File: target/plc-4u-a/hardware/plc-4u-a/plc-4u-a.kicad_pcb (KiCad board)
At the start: 2 copper layers, 363.5 x 84 mm, 216 parts, among them J1 Screw_Terminal_01x02, J10 AUX_INS, J11 X Leds Btns, J12 S3 S5 LEDs, J13 Valve control in, J14 Leak sensors, J15 I2C, J16 I2C, J17 TA_C, J18 X leds btns, J19 Valve leds, J2 Screw_Terminal_01x02, J20 Valve leds, J21 Leak sensors, J22 Valve control in, J23 S3 S5 LEDs, J24 S4 S6 LEDs, J25 S3 S5 LEDs, J26 S4 S6 LEDs, J27 S3BTN, J28 S4BTN, J29 S5BTN, J3 Screw_Terminal_01x02, J30 S6BTN, J31 S3BTN, J32 S4BTN, J33 S5BTN, J34 S6BTN, J35 PWR_OUT, J36 Sensors AB, J37 Sensors CD, J38 PWR_OUT, J39 Leak sensors, J4 Screw_Terminal_01x02, J40 Leak sensors, J41 TA_C, J42 TB_C, J43 TC_C, J44 TD_C, J45 TB_C, J46 TC_C, J47 TD_C, J48 S3 S5 LEDs, J49 S1 S2 LEDs, J5 Screw_Terminal_01x02, J50 S1 S2 BTNS, J51 X0, J52 U8 IN, J53 X0, J54 X9 IN, J55 AVR-ISP-10, J56 U17 OUT, J57 U8 OUT, J58 U17 OUT, J59 U8 OUT, J6 V_ST_HWS, J60 GND, J61 GND, J62 VCC, J63 VCC, J64 SIM800, J65 RES_IN, J66 SELF_PWR_IN, J67 VDD VSS, J68 VDD VSS, J69 VDD, J7 V_ST_CWS, J70 VDD, J71 RESERVED_OUT, J72 VSS, J73 VSS, J74 VSS, J75 VSS, J76 VSS, J77 VDD, J78 VDD, J79 NC, J8 W_CT_HWS, J80 NC, J81 NC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

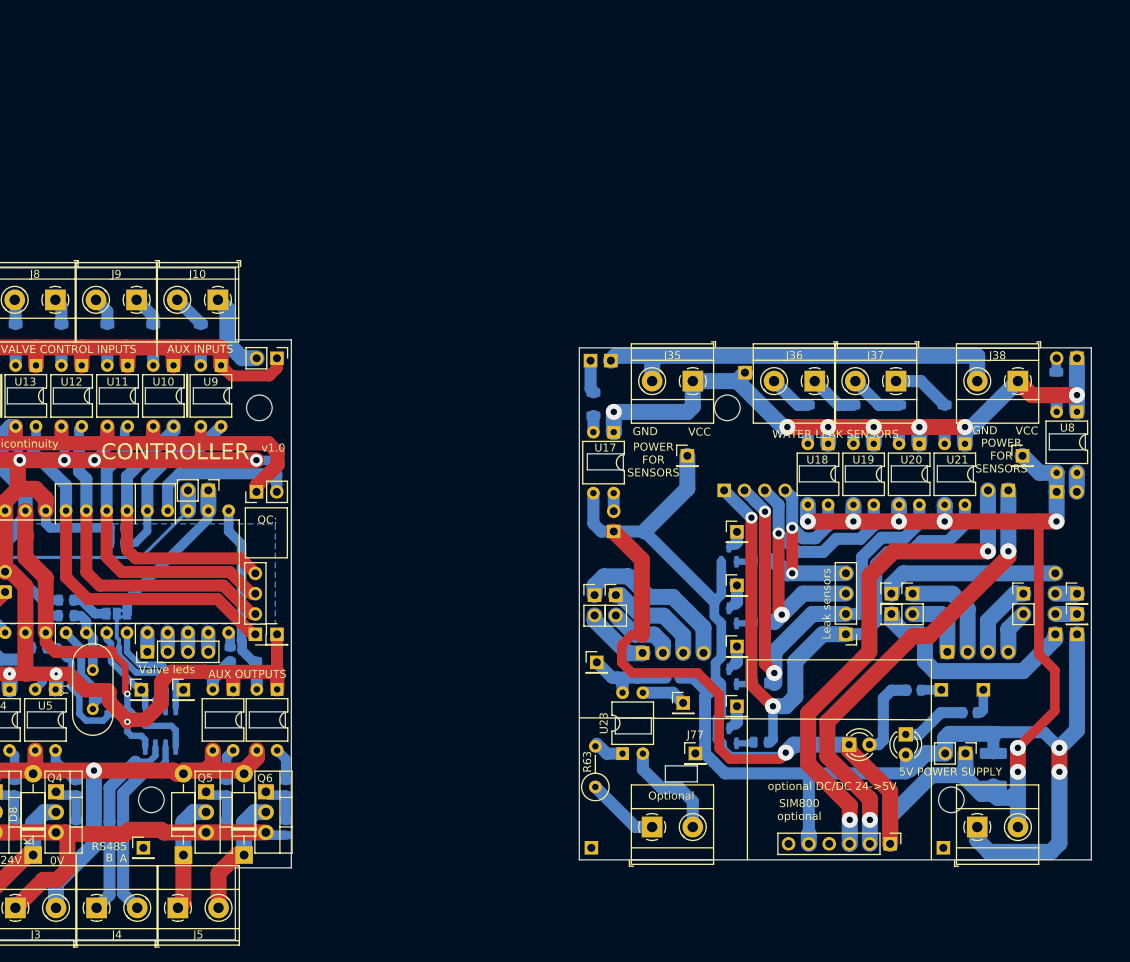
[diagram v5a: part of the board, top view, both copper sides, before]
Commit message: plc-4u-a board += RS485 protection
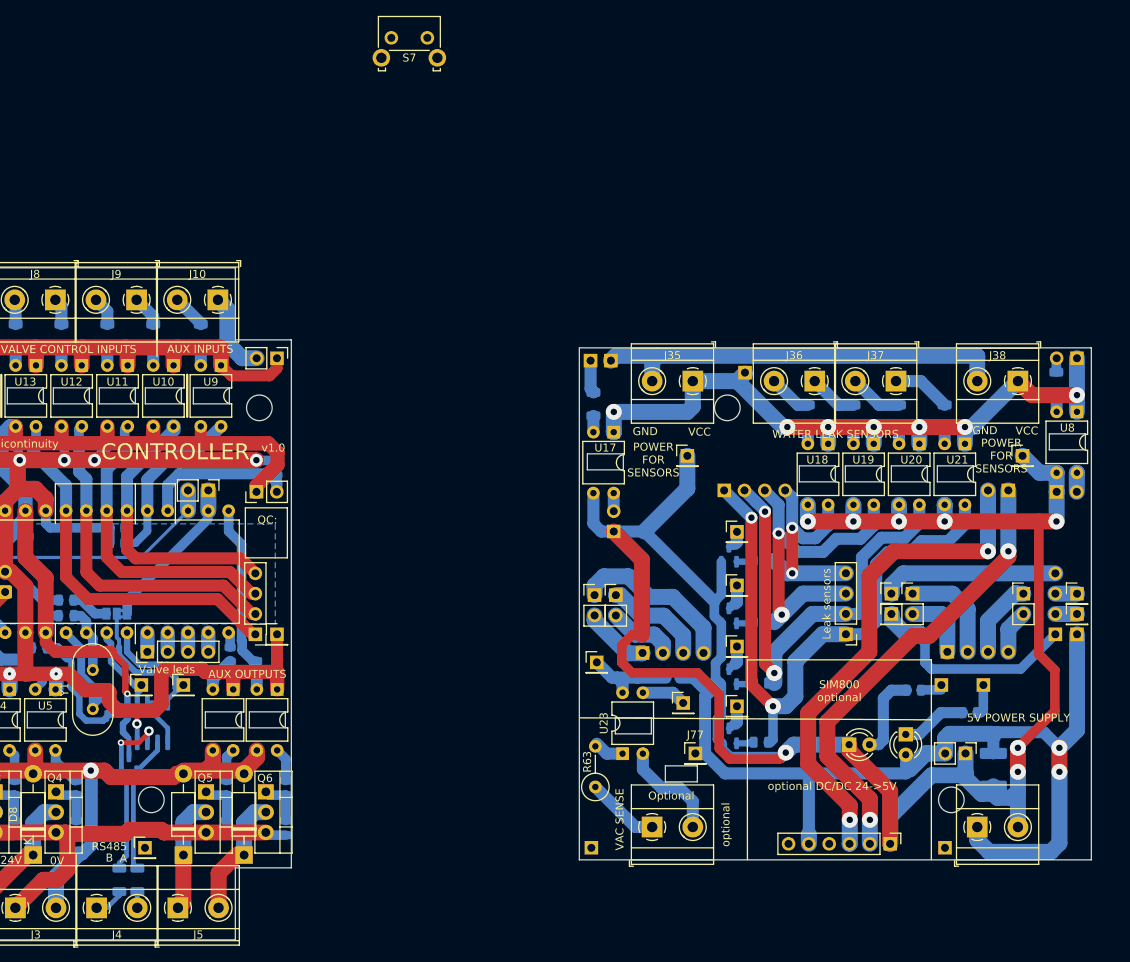
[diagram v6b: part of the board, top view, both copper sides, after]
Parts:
- added D13: PESD2CAN, Package_TO_SOT_SMD:SOT-23, B.Cu at (111.7, 120.0)
- added R66: 10, Resistor_SMD:R_1206_3216Metric, B.Cu at (112.8, 134.5)
- added R67: 10, Resistor_SMD:R_1206_3216Metric, B.Cu at (110.5, 134.5)
- added S7: MOMENTARY-SWITCH-SPST-PTH-6.0MM, Button_Switch_THT:SW_Tactile_SKHH_Angled, F.Cu at (144.5, 29.2)
- moved U22 1.17 mm to (114.6, 114.8)
- moved J83 0.60 mm to (113.2, 110.2)
- moved J84 0.60 mm to (213.2, 110.2)
- moved J85 0.60 mm to (118.5, 110.2)
- moved J86 0.60 mm to (218.5, 110.2)
- moved J81 0.20 mm to (113.7, 130.5)
- moved J82 0.20 mm to (213.7, 130.5)
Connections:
- U22 pad 6: /A -> /AA
- U22 pad 7: /B -> /BB
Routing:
- net /BB: track 0.00 -> 22.0 mm, vias 0 -> 2
- net /A: track 23.8 -> 2.04 mm
- net /B: track 24.2 -> 3.97 mm
- net /AA: track 0.00 -> 17.2 mm
- net /VSS: track 232.2 -> 239.8 mm
- net /VDD: track 206.4 -> 205.2 mm
- net Net-(JP1-Pad2): track 18.1 -> 17.1 mm
- net /TXD: track 13.8 -> 13.1 mm
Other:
- board text added: "VAC SENSE"
- board text added: "optional"

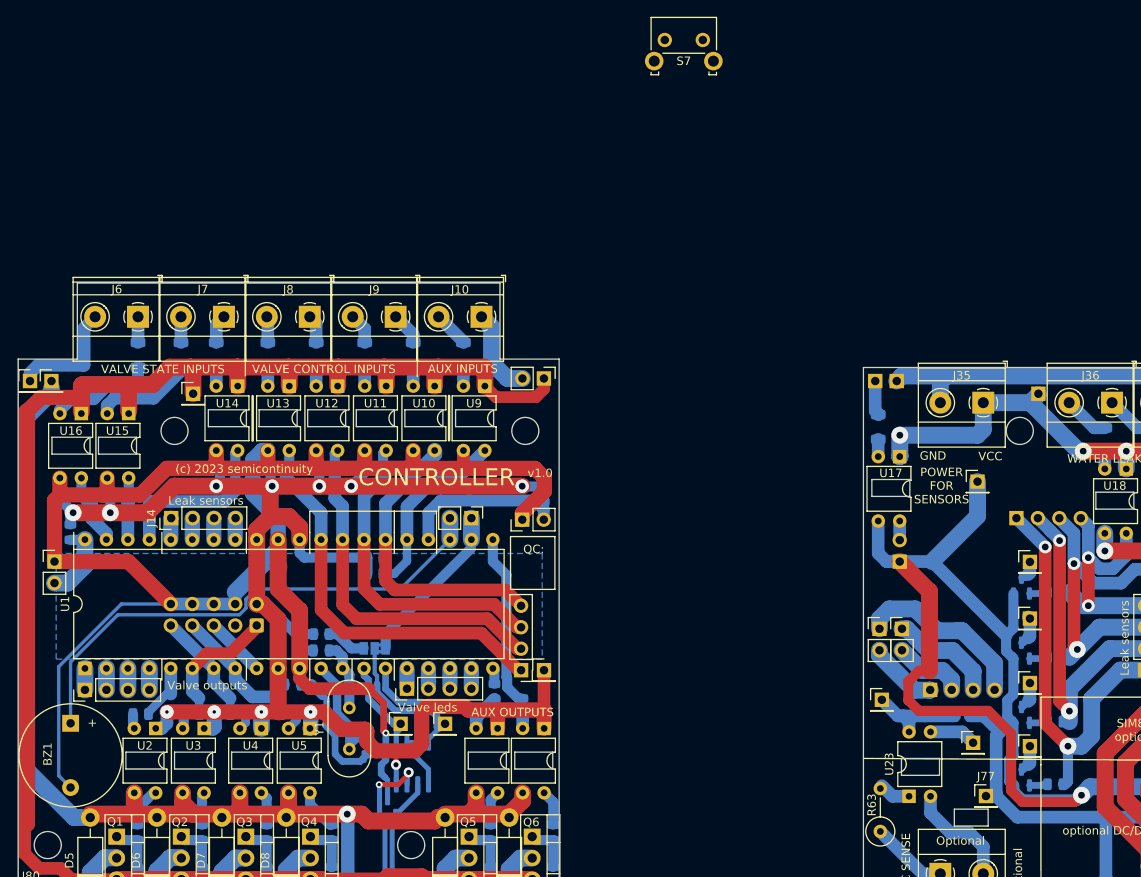
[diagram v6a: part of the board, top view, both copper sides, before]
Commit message: plc4u-a: main-retained-register (preparing for buzzer)
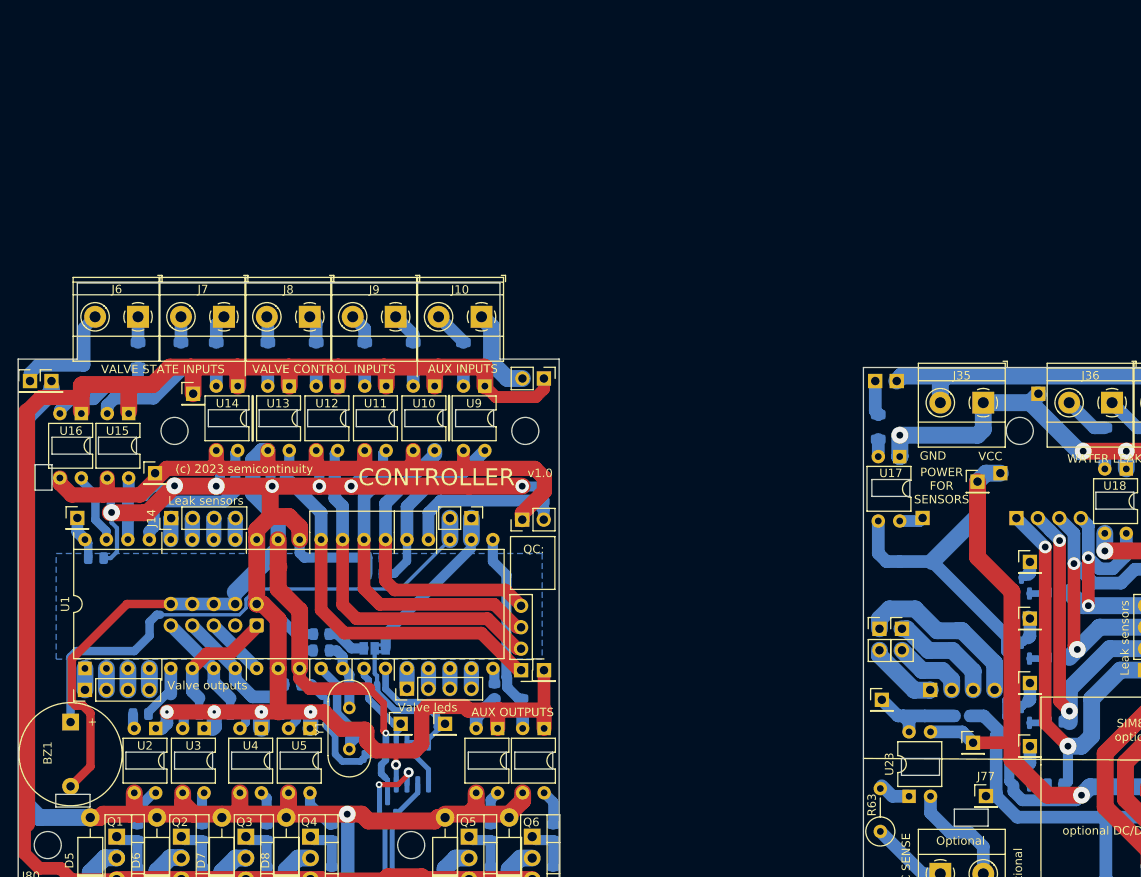
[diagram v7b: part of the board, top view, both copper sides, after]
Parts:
- removed S7: MOMENTARY-SWITCH-SPST-PTH-6.0MM, Button_Switch_THT:SW_Tactile_SKHH_Angled
- added J87: VSS, Connector_PinHeader_2.54mm:PinHeader_1x01_P2.54mm_Vertical, F.Cu at (84.2, 80.5)
- added J88: VSS, Connector_PinHeader_2.54mm:PinHeader_1x01_P2.54mm_Vertical, B.Cu at (184.2, 80.5)
- J56: value U17 OUT -> PA0; footprint Connector_PinHeader_2.54mm:PinHeader_1x02_P2.54mm_Vertical -> Connector_PinHeader_2.54mm:PinHeader_1x01_P2.54mm_Vertical
- J58: value U17 OUT -> NC; footprint Connector_PinHeader_2.54mm:PinHeader_1x02_P2.54mm_Vertical -> Connector_PinHeader_2.54mm:PinHeader_1x01_P2.54mm_Vertical
- J71: value RESERVED_OUT -> RESERVED_IN
- moved J56 5.83 mm to (175.0, 85.8), turned to 180 degrees
- moved J58 5.83 mm to (75.0, 85.8)
- moved R59 4.31 mm to (77.2, 90.5), turned to 0 degrees
- moved R15 3.84 mm to (78.0, 83.1), turned to 0 degrees
- moved R14 2.19 mm to (82.0, 83.1), turned to 0 degrees
- moved BZ1 0.14 mm to (74.2, 110.0)
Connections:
- J56 pad 1: /Middle board/VSS -> /Middle board/PA0
- J58 pad 1: /VSS -> /PA0
- J72 pad 1: Net-(J72-Pad1) -> /Middle board/VSS
- U23 pad 3: Net-(J72-Pad1) -> /Middle board/VSS
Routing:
- net /VSS: track 239.8 -> 215.6 mm
- net /Middle board/VSS: track 259.4 -> 267.9 mm
- net Net-(J72-Pad1): track 5.57 -> 0.00 mm
- net /PA0: track 9.28 -> 5.33 mm
- net /VDD: track 205.2 -> 207.6 mm
- net /GND: track 143.5 -> 145.8 mm
- net /SDA: track 61.3 -> 62.5 mm
- net /PA3: track 19.9 -> 19.3 mm
- net /Middle board/PA0: track 2.26 -> 2.85 mm
- net /PA1: track 9.05 -> 8.52 mm
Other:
- outline, holes or cut-outs redrawn
- board text added: "to be connected by wire"
